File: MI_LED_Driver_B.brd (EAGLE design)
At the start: 39.4 x 25.4 mm, 23 parts, among them IC1 LT3517, J1 HDR-1X1-14AWG, J2 HDR-1X1-14AWG, J3 HDR-1X1-18AWG_WIRE, J5 HDR-1X1-14AWG

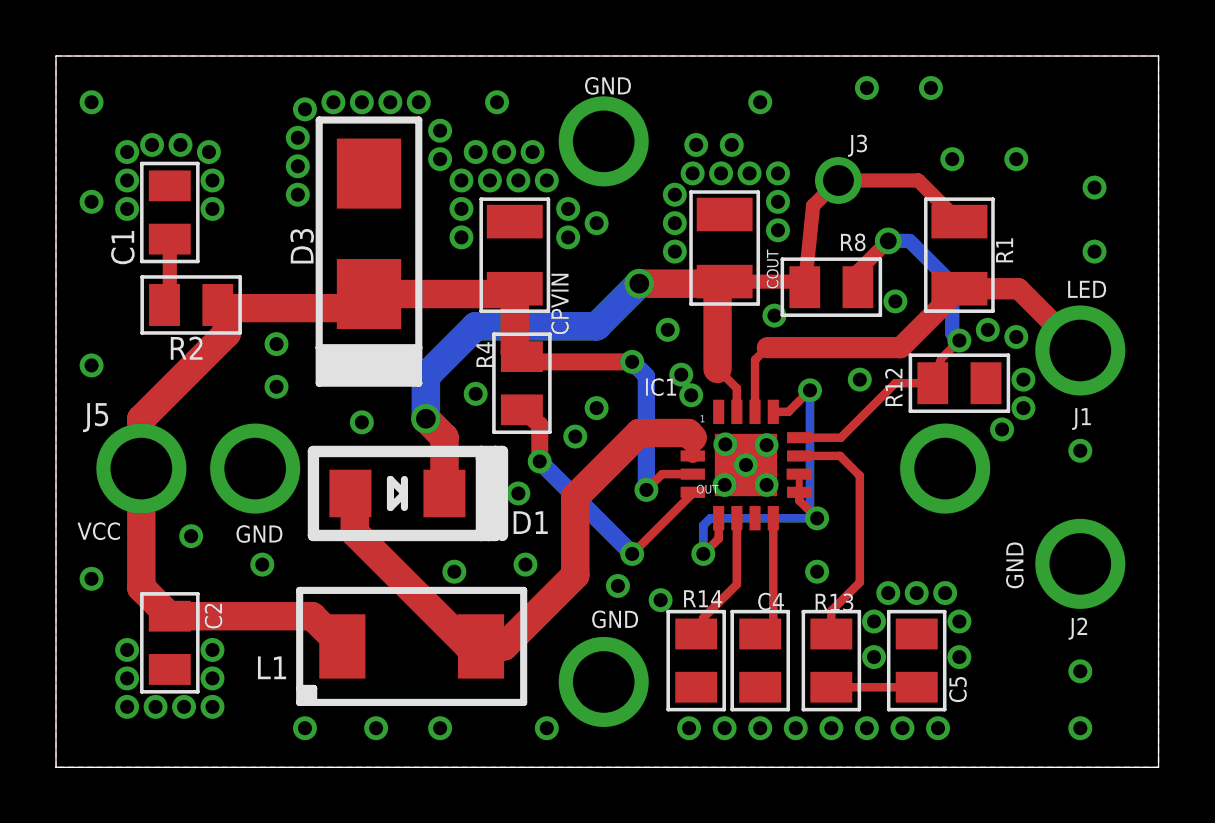
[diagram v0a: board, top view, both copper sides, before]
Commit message: Updates with correct part sizes
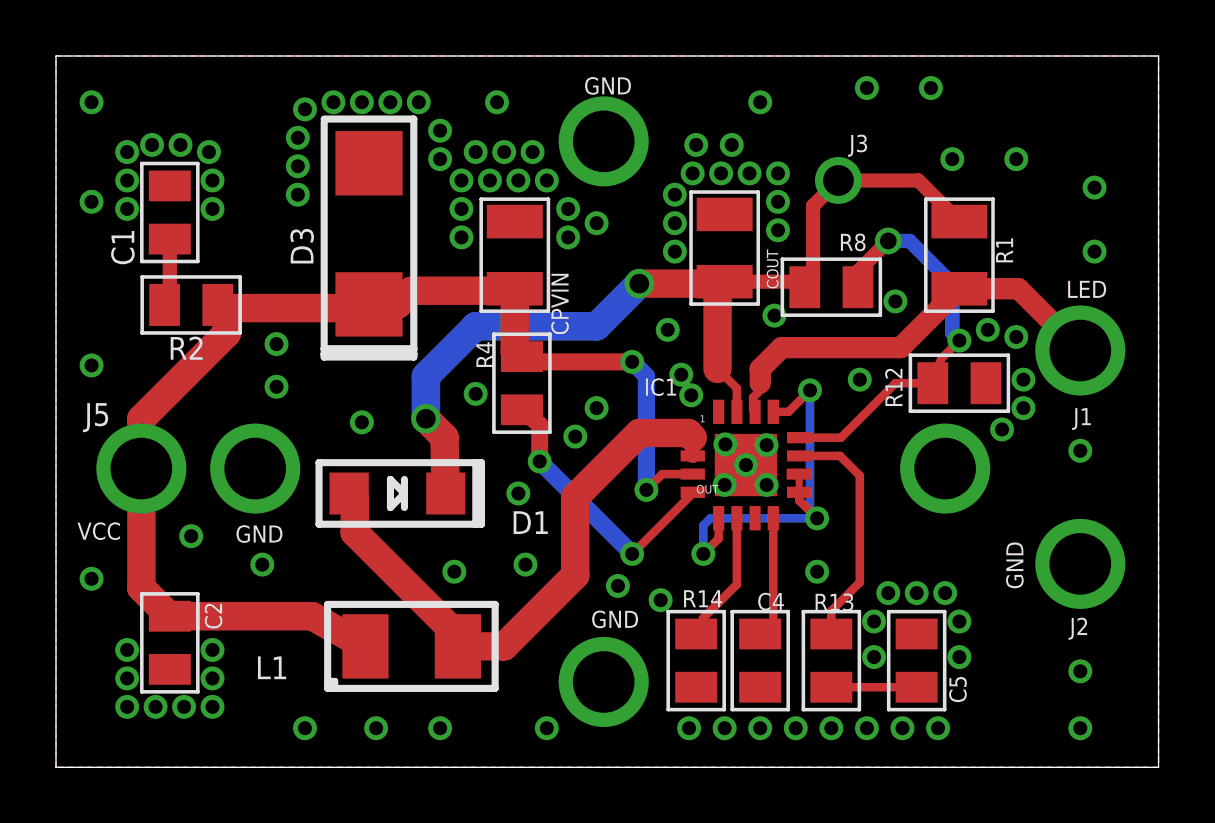
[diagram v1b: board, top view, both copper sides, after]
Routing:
- net VIN: track 43.9 -> 45.1 mm
- net N$5: track 20.7 -> 21.4 mm
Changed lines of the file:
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@@
 <wire x1="4.064" y1="5.395" x2="3.048" y2="6.411" width="1.016" layer="1"/>
 <wire x1="4.064" y1="5.395" x2="9.148" y2="5.395" width="1.016" layer="1"/>
-<wire x1="9.148" y1="5.395" x2="10.225" y2="4.318" width="1.016" layer="1"/>
+<wire x1="9.148" y1="5.395" x2="11.05" y2="4.318" width="1.016" layer="1"/>
 <wire x1="3.048" y1="10.668" x2="3.048" y2="12.446" width="1.016" layer="1"/>
 <wire x1="3.048" y1="12.446" x2="6.096" y2="15.494" width="1.016" layer="1"/>
 <wire x1="6.096" y1="16.398" x2="5.776" y2="16.51" width="1.016" layer="1"/>
-<wire x1="11.058" y1="17.018" x2="11.176" y2="16.9" width="1.016" layer="1"/>
-<wire x1="11.176" y1="16.9" x2="16.195" y2="16.9" width="1.016" layer="1"/>
+<wire x1="11.058" y1="17.018" x2="11.176" y2="16.53" width="1.016" layer="1"/>
 <wire x1="16.195" y1="16.9" x2="16.383" y2="17.088" width="1.016" layer="1"/>
 <wire x1="16.383" y1="17.088" x2="16.383" y2="14.82" width="1.016" layer="1"/>
@@
 <wire x1="6.096" y1="16.19" x2="5.776" y2="16.51" width="1.016" layer="1"/>
 <wire x1="6.096" y1="16.398" x2="10.674" y2="16.398" width="1.016" layer="1"/>
-<wire x1="10.674" y1="16.398" x2="11.176" y2="16.9" width="1.016" layer="1"/>
+<wire x1="10.674" y1="16.398" x2="11.176" y2="16.53" width="1.016" layer="1"/>
+<wire x1="11.176" y1="16.53" x2="12.212" y2="16.53" width="1.016" layer="1"/>
+<wire x1="12.212" y1="16.53" x2="12.7" y2="17.018" width="1.016" layer="1"/>
+<wire x1="12.7" y1="17.018" x2="16.313" y2="17.018" width="1.016" layer="1"/>
+<wire x1="16.313" y1="17.018" x2="16.383" y2="17.088" width="1.016" layer="1"/>
 </signal>
 <signal name="GND">
@@
 <contactref element="L1" pad="NO_DOT"/>
 <wire x1="22.738" y1="11.77" x2="22.738" y2="11.12" width="0.508" layer="1"/>
-<wire x1="15.175" y1="4.318" x2="14.732" y2="4.318" width="1.016" layer="1"/>
-<wire x1="14.732" y1="4.318" x2="10.668" y2="8.382" width="1.016" layer="1"/>
-<wire x1="10.668" y1="8.382" x2="10.668" y2="9.623" width="1.016" layer="1"/>
-<wire x1="10.668" y1="9.623" x2="10.512" y2="9.779" width="1.016" layer="1"/>
-<wire x1="15.175" y1="4.318" x2="16.002" y2="4.318" width="1.016" layer="1"/>
+<wire x1="10.668" y1="9.623" x2="10.467" y2="9.779" width="1.016" layer="1"/>
+<wire x1="14.35" y1="4.318" x2="14.732" y2="4.318" width="1.016" layer="1"/>
+<wire x1="14.732" y1="4.318" x2="16.002" y2="4.318" width="1.016" layer="1"/>
 <wire x1="16.002" y1="4.318" x2="18.542" y2="6.858" width="1.016" layer="1"/>
 <wire x1="18.542" y1="6.858" x2="18.542" y2="9.652" width="1.016" layer="1"/>
@@
 <wire x1="20.828" y1="11.938" x2="22.57" y2="11.938" width="1.016" layer="1"/>
 <wire x1="22.57" y1="11.938" x2="22.738" y2="11.77" width="1.016" layer="1"/>
+<wire x1="14.732" y1="4.318" x2="10.668" y2="8.382" width="1.016" layer="1"/>
+<wire x1="10.668" y1="8.382" x2="10.668" y2="9.578" width="1.016" layer="1"/>
+<wire x1="10.668" y1="9.578" x2="10.467" y2="9.779" width="1.016" layer="1"/>
 </signal>
 <signal name="N$11">
@@
 <wire x1="23.876" y1="17.342" x2="26.839" y2="17.342" width="0.508" layer="1"/>
 <wire x1="26.839" y1="17.342" x2="26.736" y2="17.145" width="0.3048" layer="1"/>
-<wire x1="26.736" y1="17.145" x2="27.036" y2="20.051" width="0.508" layer="1"/>
 <wire x1="27.036" y1="20.051" x2="27.94" y2="20.955" width="0.508" layer="1"/>
 <wire x1="27.94" y1="20.955" x2="30.791" y2="20.955" width="0.508" layer="1"/>
 <wire x1="30.791" y1="20.955" x2="32.258" y2="19.488" width="0.508" layer="1"/>
-<wire x1="13.872" y1="9.779" x2="13.872" y2="11.782" width="1.016" layer="1"/>
+<wire x1="13.917" y1="9.779" x2="13.872" y2="11.782" width="1.016" layer="1"/>
 <wire x1="13.872" y1="11.782" x2="13.208" y2="12.446" width="1.016" layer="1"/>
 <wire x1="13.208" y1="12.446" x2="13.208" y2="13.97" width="1.016" layer="16"/>
@@
 <via x="13.208" y="12.446" extent="1-16" drill="0.7"/>
 <via x="20.828" y="17.272" extent="1-16" drill="0.7"/>
+<wire x1="27.036" y1="20.051" x2="27.036" y2="17.445" width="0.508" layer="1"/>
+<wire x1="27.036" y1="17.445" x2="26.736" y2="17.145" width="0.508" layer="1"/>
 </signal>
 <signal name="N$1">
@@
 <contactref element="R1" pad="2"/>
 <contactref element="J1" pad="P$1"/>
-<wire x1="25.4" y1="14.986" x2="30.156" y2="14.986" width="0.762" layer="1"/>
+<wire x1="25.908" y1="14.986" x2="30.156" y2="14.986" width="0.762" layer="1"/>
 <wire x1="30.156" y1="14.986" x2="32.258" y2="17.088" width="0.762" layer="1"/>
 <wire x1="32.258" y1="17.088" x2="34.3724" y2="17.088" width="0.762" layer="1"/>
 <wire x1="34.3724" y1="17.088" x2="36.576" y2="14.8844" width="0.762" layer="1"/>
-<wire x1="24.963" y1="12.695" x2="24.963" y2="14.549" width="0.3048" layer="1"/>
-<wire x1="24.963" y1="14.549" x2="25.4" y2="14.986" width="0.3048" layer="1"/>
+<wire x1="25.146" y1="13.716" x2="25.146" y2="13.462" width="0.3048" layer="1"/>
+<wire x1="25.146" y1="13.462" x2="24.892" y2="13.208" width="0.3048" layer="1"/>
+<wire x1="24.892" y1="13.208" x2="24.892" y2="12.766" width="0.3048" layer="1"/>
+<wire x1="24.892" y1="12.766" x2="24.963" y2="12.695" width="0.3048" layer="1"/>
+<wire x1="25.146" y1="13.716" x2="25.146" y2="14.224" width="0.762" layer="1"/>
+<wire x1="25.146" y1="14.224" x2="25.908" y2="14.986" width="0.762" layer="1"/>
 </signal>
 <signal name="N$10">
